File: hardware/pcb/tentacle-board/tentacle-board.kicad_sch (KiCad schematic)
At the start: 39 parts, among them J1 USB_B_Micro, J2 Conn_01x02, J3 Conn_02x18_Odd_Even, J4 Conn_02x18_Odd_Even, J5 Motor 1, U1 NCP1117-3.3_SOT223, U2 W25Q128JVS, U3 RP2040, U4 DRV8825PWP, Y1 ABLS-12.000MHZ-B4-T

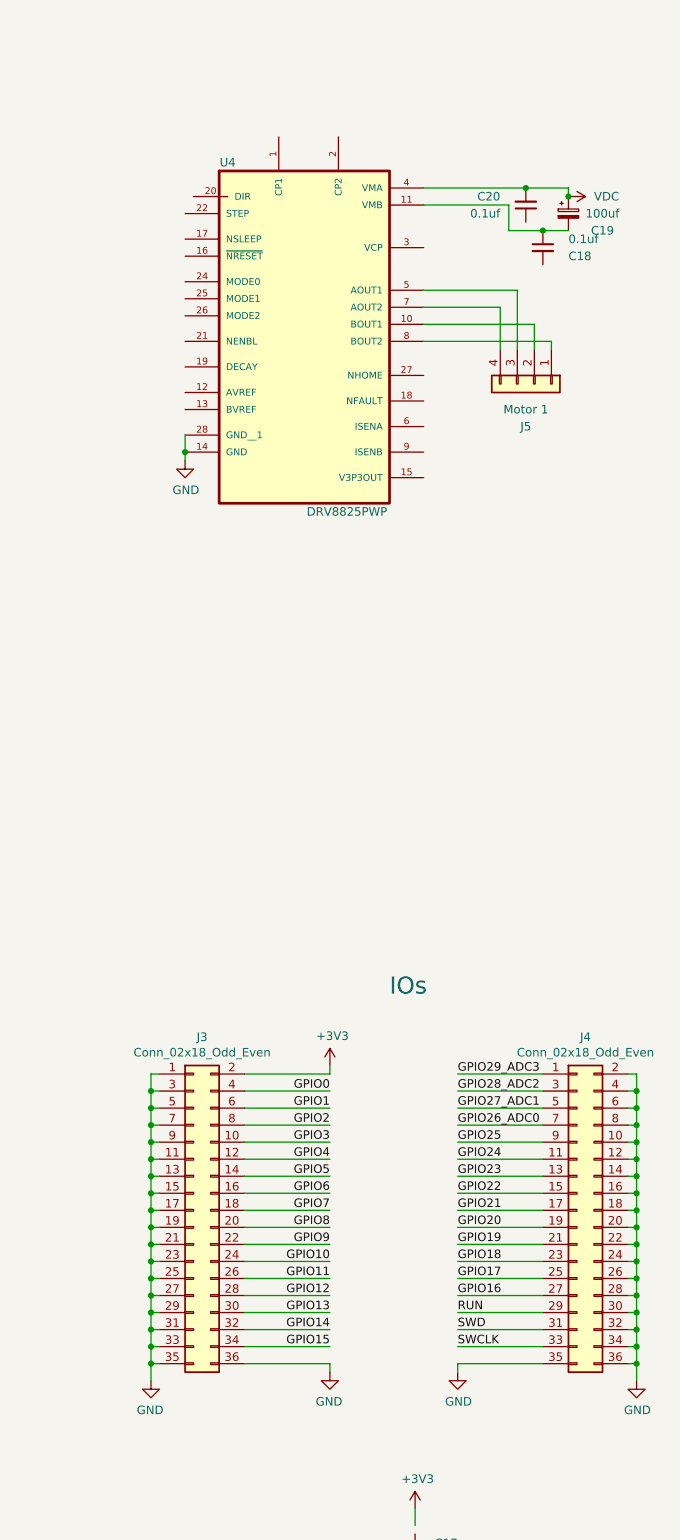
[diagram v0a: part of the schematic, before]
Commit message: Added stepper drivers to the tentacle controller PCB
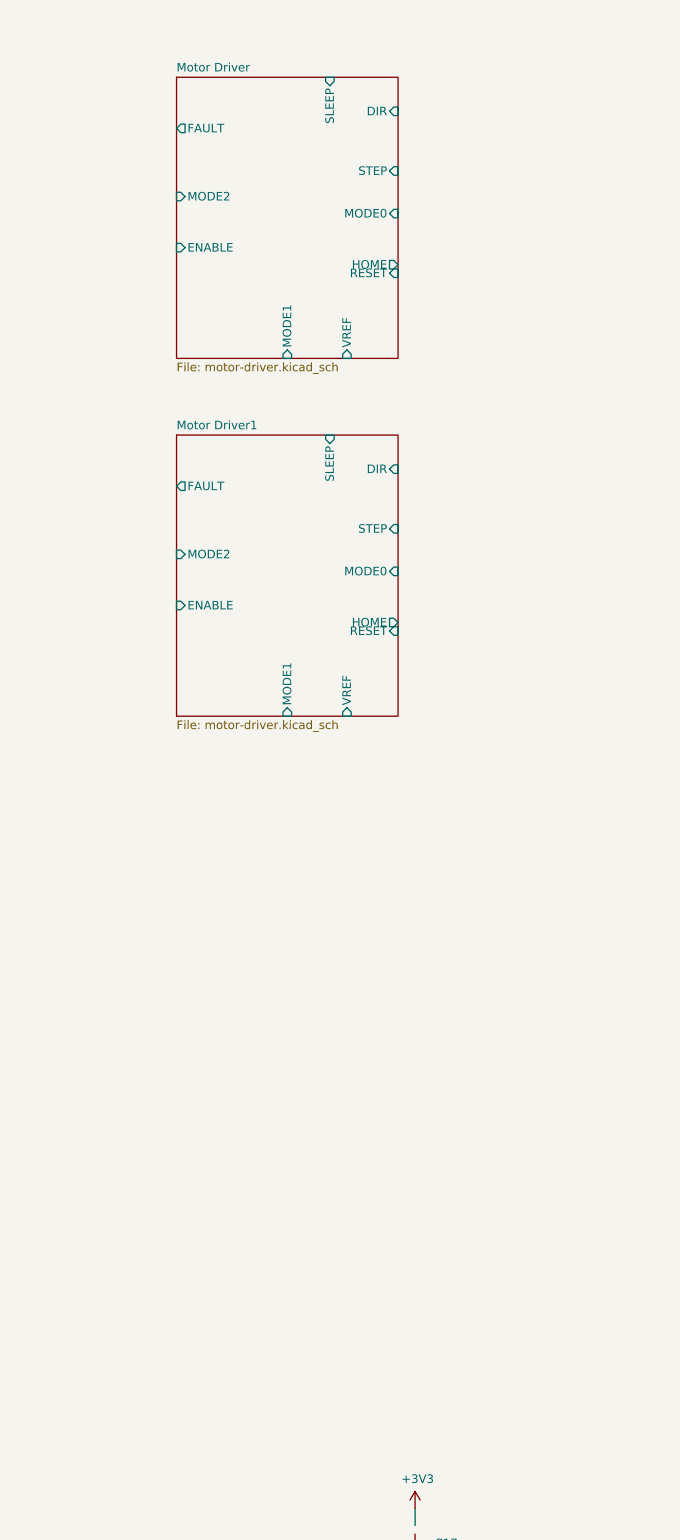
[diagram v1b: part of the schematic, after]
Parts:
- removed C18, C20: 0.1uf, Capacitor_SMD:C_0805_2012Metric_Pad1.18x1.45mm_HandSolder, symbol Device:C_Small
- removed C19: 100uf, Capacitor_THT:CP_Radial_D6.3mm_P2.50mm, symbol Device:C_Polarized_Small
- removed J3, J4: Conn_02x18_Odd_Even, Connector_PinHeader_2.54mm:PinHeader_2x18_P2.54mm_Vertical, symbol Connector_Generic:Conn_02x18_Odd_Even
- removed J5: Motor 1, Connector_JST:JST_XH_B4B-XH-A_1x04_P2.50mm_Vertical, symbol Connector_Generic:Conn_01x04
- removed U4: DRV8825PWP, IC_TPS61196PWPRQ1, symbol DRV8825PWP:DRV8825PWP
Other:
- added sheet Motor Driver (motor-driver.kicad_sch)
- added sheet Motor Driver1 (motor-driver.kicad_sch)
- note removed: "IOs"

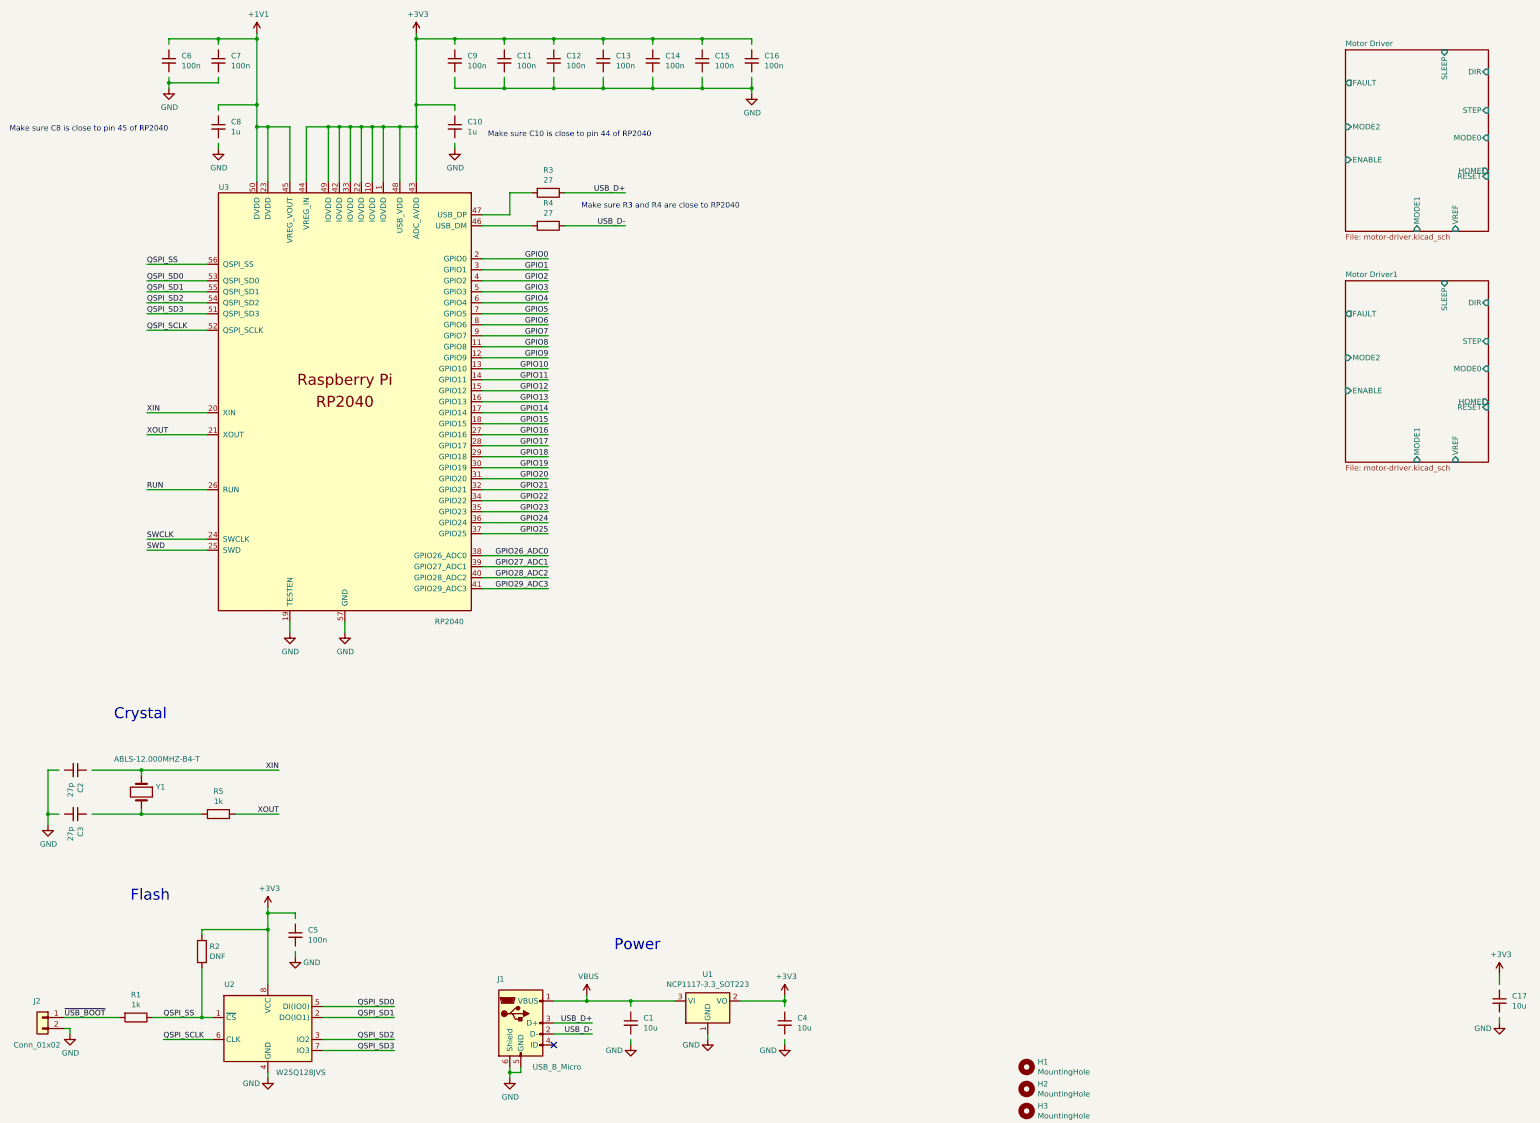
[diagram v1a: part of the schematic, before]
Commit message: Worked on the motor power system and stepper driver BOM
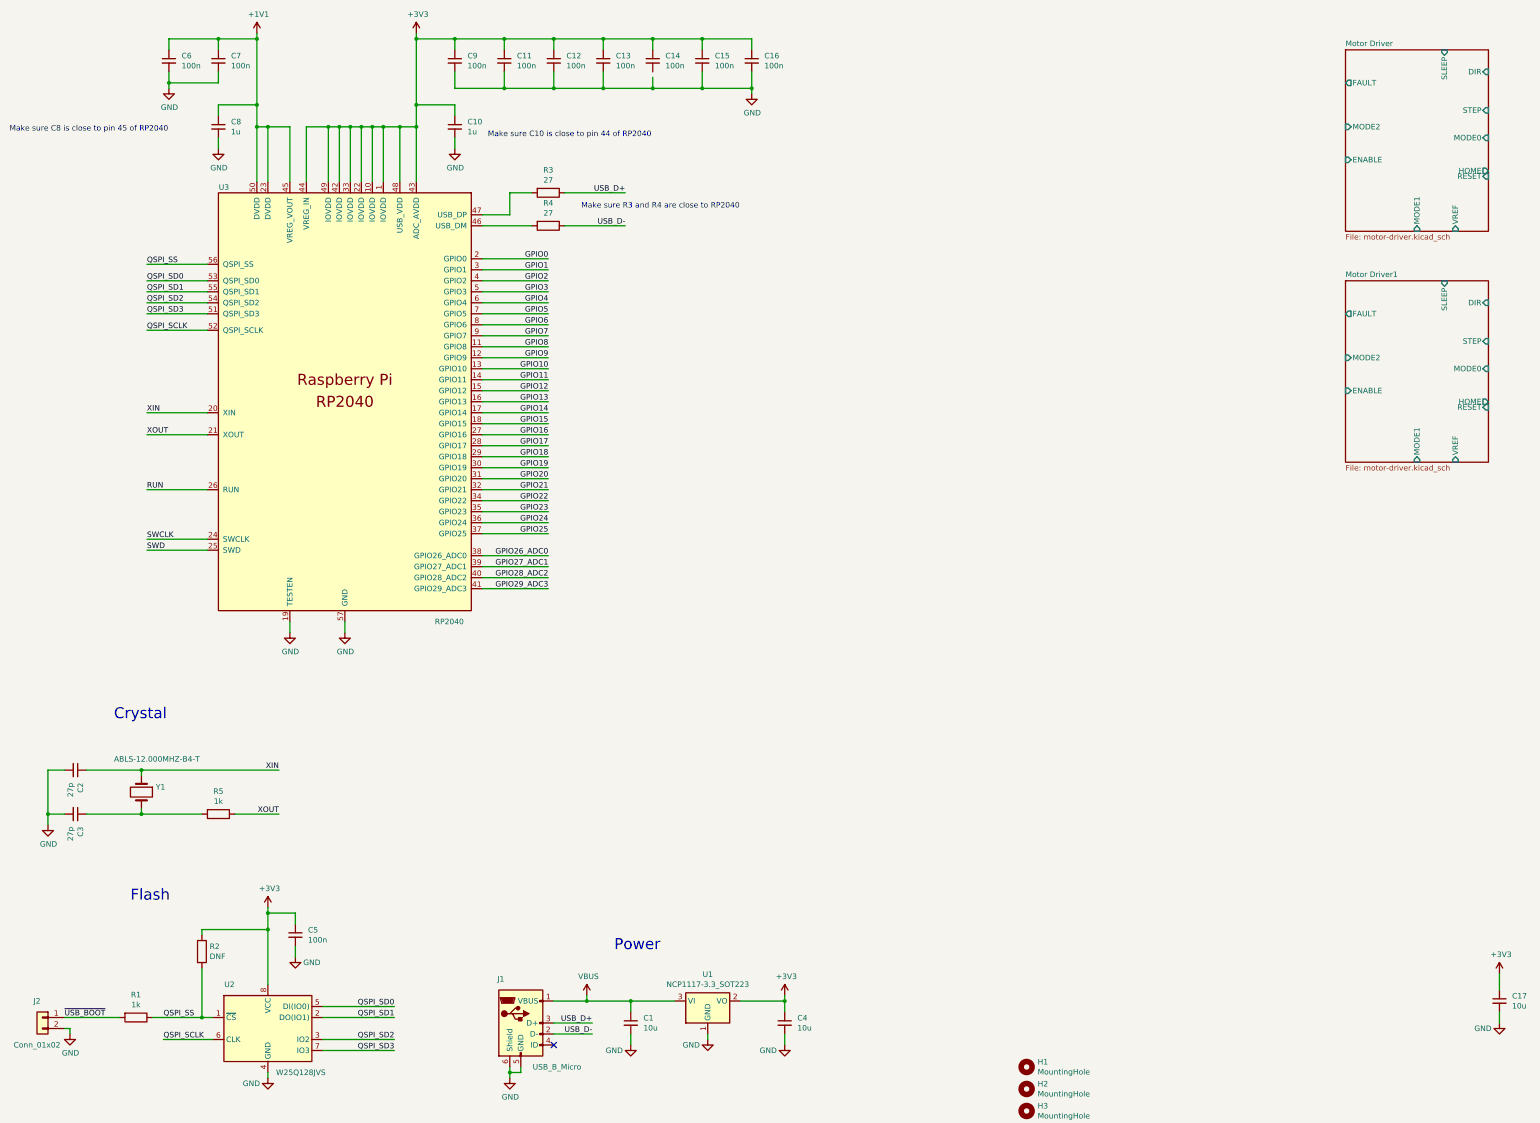
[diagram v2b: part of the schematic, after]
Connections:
- net +1V1: now also C6.1, C7.1, C8.1
- net +3V3: now also C10.1, C11.1, C12.1, C13.1, C14.1, C15.1, C16.1, C17.1, C4.1, C5.1, C9.1
- net GND: now also C1.2, C10.2, C11.2, C12.2, C13.2, C15.2, C16.2, C17.2, C2.2, C3.2, C4.2, C5.2, C6.2, C7.2, C8.2, C9.2
- net VBUS: now also C1.1
- net XIN: now also C2.1
- net at C3.1: now also R5.2, Y1.2
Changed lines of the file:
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@@
-    (stroke (width 0) (type default))
-  )
-  (wire (pts (xy 195.58 245.11) (xy 195.58 243.84))
     (stroke (width 0) (type default))
   )
@@
     (stroke (width 0) (type default))
   )
-  (wire (pts (xy 160.02 245.11) (xy 160.02 243.84))
+  (wire (pts (xy 160.02 243.84) (xy 160.02 246.38))
     (stroke (width 0) (type default))
   )
@@
     (stroke (width 0) (type default))
   )
-  (wire (pts (xy 64.77 45.72) (xy 64.77 46.99))
+  (wire (pts (xy 64.77 44.45) (xy 64.77 46.99))
     (stroke (width 0) (type default))
   )
@@
     (stroke (width 0) (type default))
   )
-  (wire (pts (xy 119.38 38.1) (xy 119.38 36.83))
+  (wire (pts (xy 119.38 36.83) (xy 119.38 39.37))
     (stroke (width 0) (type default))
   )
@@
     (stroke (width 0) (type default))
   )
+  (wire (pts (xy 142.24 21.59) (xy 142.24 24.13))
+    (stroke (width 0) (type default))
+  )
   (wire (pts (xy 76.2 41.91) (xy 73.66 41.91))
     (stroke (width 0) (type default))
@@
     (stroke (width 0) (type default))
   )
-  (wire (pts (xy 165.1 22.86) (xy 165.1 21.59))
+  (wire (pts (xy 165.1 21.59) (xy 165.1 24.13))
     (stroke (width 0) (type default))
   )
@@
     (stroke (width 0) (type default))
   )
-  (wire (pts (xy 27.94 200.66) (xy 25.4 200.66))
+  (wire (pts (xy 25.4 200.66) (xy 29.21 200.66))
     (stroke (width 0) (type default))
   )
@@
     (stroke (width 0) (type default))
   )
-  (wire (pts (xy 35.56 190.5) (xy 46.99 190.5))
+  (wire (pts (xy 34.29 190.5) (xy 46.99 190.5))
     (stroke (width 0) (type default))
   )
@@
     (stroke (width 0) (type default))
   )
-  (wire (pts (xy 153.67 30.48) (xy 153.67 33.02))
+  (wire (pts (xy 153.67 29.21) (xy 153.67 33.02))
     (stroke (width 0) (type default))
   )
@@
     (stroke (width 0) (type default))
   )
-  (wire (pts (xy 35.56 200.66) (xy 46.99 200.66))
-    (stroke (width 0) (type default))
-  )
-  (wire (pts (xy 53.34 22.86) (xy 53.34 21.59))
+  (wire (pts (xy 34.29 200.66) (xy 46.99 200.66))
+    (stroke (width 0) (type default))
+  )
+  (wire (pts (xy 53.34 21.59) (xy 53.34 24.13))
     (stroke (width 0) (type default))
   )
@@
     (stroke (width 0) (type default))
   )
-  (wire (pts (xy 360.68 237.49) (xy 360.68 240.03))
+  (wire (pts (xy 130.81 21.59) (xy 130.81 24.13))
+    (stroke (width 0) (type default))
+  )
+  (wire (pts (xy 360.68 237.49) (xy 360.68 241.3))
     (stroke (width 0) (type default))
   )
@@
     (stroke (width 0) (type default))
   )
-  (wire (pts (xy 176.53 22.86) (xy 176.53 21.59))
+  (wire (pts (xy 176.53 21.59) (xy 176.53 24.13))
     (stroke (width 0) (type default))
   )
@@
     (stroke (width 0) (type default))
   )
-  (wire (pts (xy 64.77 38.1) (xy 64.77 36.83))
+  (wire (pts (xy 64.77 36.83) (xy 64.77 39.37))
     (stroke (width 0) (type default))
   )
@@
     (stroke (width 0) (type default))
   )
+  (wire (pts (xy 195.58 251.46) (xy 195.58 254))
+    (stroke (width 0) (type default))
+  )
   (wire (pts (xy 88.9 247.65) (xy 105.41 247.65))
     (stroke (width 0) (type default))
   )
-  (wire (pts (xy 195.58 252.73) (xy 195.58 254))
-    (stroke (width 0) (type default))
-  )
   (wire (pts (xy 125.73 113.03) (xy 140.97 113.03))
     (stroke (width 0) (type default))
@@
     (stroke (width 0) (type default))
   )
-  (wire (pts (xy 187.96 30.48) (xy 187.96 33.02))
-    (stroke (width 0) (type default))
-  )
   (wire (pts (xy 125.73 97.79) (xy 140.97 97.79))
     (stroke (width 0) (type default))
@@
     (stroke (width 0) (type default))
   )
-  (wire (pts (xy 130.81 30.48) (xy 130.81 33.02))
-    (stroke (width 0) (type default))
-  )
-  (wire (pts (xy 153.67 22.86) (xy 153.67 21.59))
+  (wire (pts (xy 153.67 21.59) (xy 153.67 24.13))
     (stroke (width 0) (type default))
   )
@@
     (stroke (width 0) (type default))
   )
+  (wire (pts (xy 53.34 29.21) (xy 53.34 31.75))
+    (stroke (width 0) (type default))
+  )
   (wire (pts (xy 110.49 36.83) (xy 110.49 41.91))
     (stroke (width 0) (type default))
@@
     (stroke (width 0) (type default))
   )
-  (wire (pts (xy 119.38 22.86) (xy 119.38 21.59))
+  (wire (pts (xy 187.96 29.21) (xy 187.96 33.02))
+    (stroke (width 0) (type default))
+  )
+  (wire (pts (xy 119.38 21.59) (xy 119.38 24.13))
     (stroke (width 0) (type default))
   )
@@
     (stroke (width 0) (type default))
   )
-  (wire (pts (xy 27.94 190.5) (xy 25.4 190.5))
+  (wire (pts (xy 25.4 190.5) (xy 29.21 190.5))
     (stroke (width 0) (type default))
   )
@@
     (stroke (width 0) (type default))
   )
-  (wire (pts (xy 119.38 45.72) (xy 119.38 46.99))
+  (wire (pts (xy 119.38 44.45) (xy 119.38 46.99))
     (stroke (width 0) (type default))
   )
@@
     (stroke (width 0) (type default))
   )
+  (wire (pts (xy 130.81 29.21) (xy 130.81 33.02))
+    (stroke (width 0) (type default))
+  )
   (wire (pts (xy 73.66 36.83) (xy 73.66 41.91))
     (stroke (width 0) (type default))
@@
     (stroke (width 0) (type default))
   )
-  (wire (pts (xy 130.81 22.86) (xy 130.81 21.59))
-    (stroke (width 0) (type default))
-  )
   (wire (pts (xy 142.24 243.84) (xy 149.86 243.84))
     (stroke (width 0) (type default))
@@
     (stroke (width 0) (type default))
   )
-  (wire (pts (xy 142.24 30.48) (xy 142.24 33.02))
-    (stroke (width 0) (type default))
-  )
   (wire (pts (xy 41.91 247.65) (xy 29.21 247.65))
     (stroke (width 0) (type default))
@@
     (stroke (width 0) (type default))
   )
-  (wire (pts (xy 142.24 22.86) (xy 142.24 21.59))
-    (stroke (width 0) (type default))
-  )
   (wire (pts (xy 46.99 191.77) (xy 46.99 190.5))
     (stroke (width 0) (type default))
@@
     (stroke (width 0) (type default))
   )
+  (wire (pts (xy 142.24 29.21) (xy 142.24 33.02))
+    (stroke (width 0) (type default))
+  )
   (wire (pts (xy 195.58 243.84) (xy 195.58 242.57))
     (stroke (width 0) (type default))
   )
-  (wire (pts (xy 53.34 30.48) (xy 53.34 31.75))
-    (stroke (width 0) (type default))
-  )
   (wire (pts (xy 125.73 82.55) (xy 140.97 82.55))
     (stroke (width 0) (type default))
@@
     (stroke (width 0) (type default))
   )
-  (wire (pts (xy 160.02 252.73) (xy 160.02 254))
+  (wire (pts (xy 160.02 251.46) (xy 160.02 254))
     (stroke (width 0) (type default))
   )
@@
     (stroke (width 0) (type default))
   )
-  (wire (pts (xy 176.53 30.48) (xy 176.53 33.02))
+  (wire (pts (xy 176.53 29.21) (xy 176.53 33.02))
     (stroke (width 0) (type default))
   )
@@
     (stroke (width 0) (type default))
   )
-  (wire (pts (xy 64.77 22.86) (xy 64.77 21.59))
+  (wire (pts (xy 64.77 21.59) (xy 64.77 24.13))
     (stroke (width 0) (type default))
   )
@@
     (stroke (width 0) (type default))
   )
-  (wire (pts (xy 119.38 30.48) (xy 119.38 33.02))
+  (wire (pts (xy 195.58 243.84) (xy 195.58 246.38))
+    (stroke (width 0) (type default))
+  )
+  (wire (pts (xy 119.38 29.21) (xy 119.38 33.02))
     (stroke (width 0) (type default))
   )
@@
     (stroke (width 0) (type default))
   )
-  (wire (pts (xy 360.68 247.65) (xy 360.68 248.92))
+  (wire (pts (xy 360.68 246.38) (xy 360.68 248.92))
     (stroke (width 0) (type default))
   )
@@
     (stroke (width 0) (type default))
   )
-  (wire (pts (xy 82.55 232.41) (xy 82.55 233.68))
+  (wire (pts (xy 82.55 231.14) (xy 82.55 233.68))
     (stroke (width 0) (type default))
   )
@@
     (stroke (width 0) (type default))
   )
-  (wire (pts (xy 82.55 224.79) (xy 82.55 223.52))
+  (wire (pts (xy 82.55 223.52) (xy 82.55 226.06))
     (stroke (width 0) (type default))
   )
@@
     (stroke (width 0) (type default))
   )
-  (wire (pts (xy 187.96 22.86) (xy 187.96 21.59))
+  (wire (pts (xy 187.96 21.59) (xy 187.96 24.13))
     (stroke (width 0) (type default))
   )
@@
     (stroke (width 0) (type default))
   )
-  (wire (pts (xy 64.77 31.75) (xy 64.77 30.48))
-    (stroke (width 0) (type default))
-  )
+  (wire (pts (xy 64.77 29.21) (xy 64.77 31.75))
+    (stroke (width 0) (type default))
+  )
